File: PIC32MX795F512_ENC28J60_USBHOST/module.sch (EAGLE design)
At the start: 75 parts, among them IC1 IC_USBLC6-2, IC2 LM1117IMPX-3.3, IC3 PIC32MX795F512, IC4 ENC28J60, T1 BC847, U1 USD-SOCKETUSD, X1 22-23-2021, X2 CRYSTALS-NOGND-CFPX-217, X3 KUSBVX, X4 22-23-2021, X5 22-23-2021, Y1 CRYSTAL-GROUNDEDSMD-5X3.2, Y2 CRYSTAL-GROUNDEDSMD-5X3.2

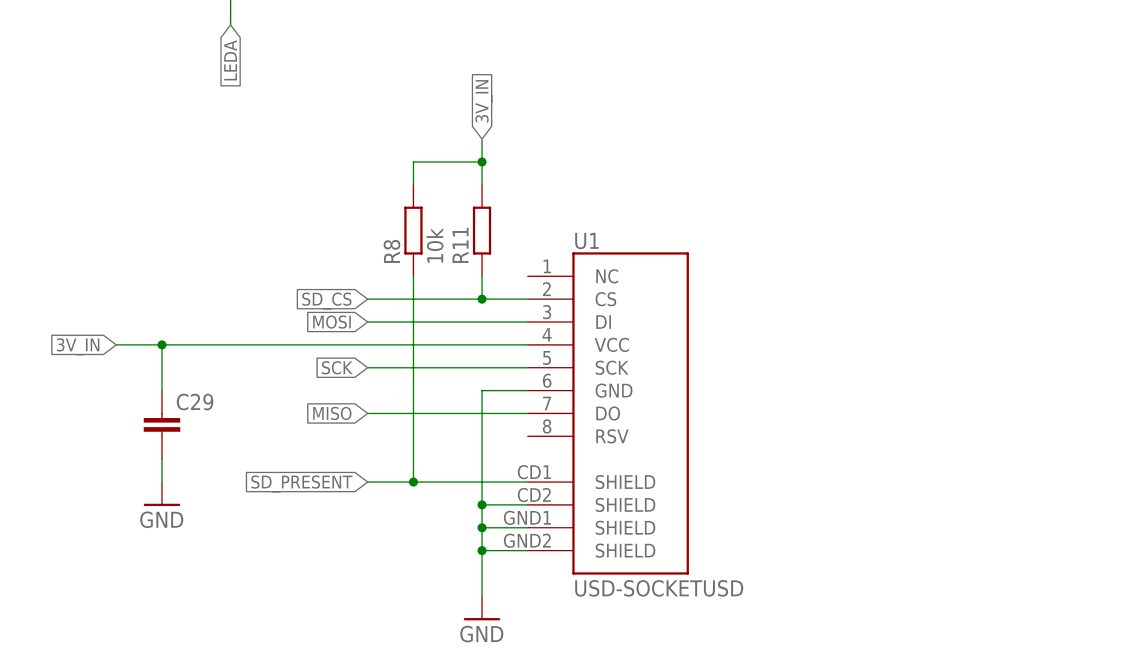
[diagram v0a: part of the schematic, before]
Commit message: MISO pull-ups added
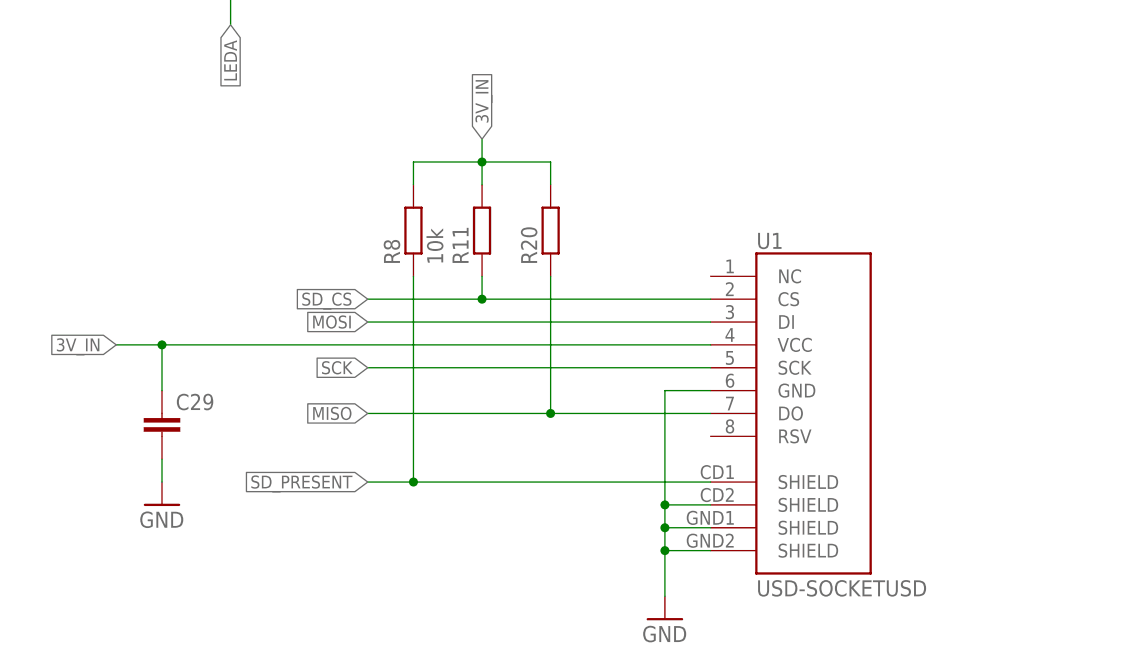
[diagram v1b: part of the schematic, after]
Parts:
- added R20: (no value), rcl:R-EU_R0603
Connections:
- net 3V_IN: now also R20.2
- net MISO: now also R20.1
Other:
- moved on the sheet: U1
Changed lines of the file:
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@@
 <part name="GND51" library="SparkFun-Aesthetics" deviceset="GND" device=""/>
 <part name="R18" library="rcl" deviceset="R-EU_" device="R0805"/>
+<part name="R20" library="rcl" deviceset="R-EU_" device="R0603"/>
 </parts>
 <sheets>
@@
 <instance part="R12" gate="G$1" x="73.66" y="83.82"/>
 <instance part="Y2" gate="G$1" x="73.66" y="157.48" rot="R90"/>
-<instance part="U1" gate="G$1" x="254" y="81.28"/>
-<instance part="GND47" gate="1" x="241.3" y="55.88"/>
+<instance part="U1" gate="G$1" x="274.32" y="81.28"/>
+<instance part="GND47" gate="1" x="261.62" y="55.88"/>
 <instance part="R11" gate="G$1" x="241.3" y="99.06" rot="R90"/>
 <instance part="C29" gate="G$1" x="205.74" y="78.74"/>
@@
 <instance part="GND51" gate="1" x="-53.34" y="535.94" rot="MR0"/>
 <instance part="R18" gate="G$1" x="104.14" y="520.7"/>
+<instance part="R20" gate="G$1" x="248.92" y="99.06" rot="R90"/>
 </instances>
 <busses>
@@
 <pinref part="GND47" gate="1" pin="GND"/>
 <pinref part="U1" gate="G$1" pin="SHIELD@4"/>
-<wire x1="241.3" y1="66.04" x2="241.3" y2="63.5" width="0.1524" layer="91"/>
-<wire x1="241.3" y1="63.5" x2="241.3" y2="58.42" width="0.1524" layer="91"/>
-<wire x1="246.38" y1="63.5" x2="241.3" y2="63.5" width="0.1524" layer="91"/>
-<junction x="241.3" y="63.5"/>
+<wire x1="261.62" y1="66.04" x2="261.62" y2="63.5" width="0.1524" layer="91"/>
+<wire x1="261.62" y1="63.5" x2="261.62" y2="58.42" width="0.1524" layer="91"/>
+<wire x1="266.7" y1="63.5" x2="261.62" y2="63.5" width="0.1524" layer="91"/>
+<junction x="261.62" y="63.5"/>
 <pinref part="U1" gate="G$1" pin="SHIELD@3"/>
-<wire x1="246.38" y1="66.04" x2="241.3" y2="66.04" width="0.1524" layer="91"/>
-<junction x="241.3" y="66.04"/>
+<wire x1="266.7" y1="66.04" x2="261.62" y2="66.04" width="0.1524" layer="91"/>
+<junction x="261.62" y="66.04"/>
 <pinref part="U1" gate="G$1" pin="GND"/>
-<wire x1="246.38" y1="81.28" x2="241.3" y2="81.28" width="0.1524" layer="91"/>
-<wire x1="241.3" y1="81.28" x2="241.3" y2="68.58" width="0.1524" layer="91"/>
+<wire x1="266.7" y1="81.28" x2="261.62" y2="81.28" width="0.1524" layer="91"/>
+<wire x1="261.62" y1="81.28" x2="261.62" y2="68.58" width="0.1524" layer="91"/>
 <pinref part="U1" gate="G$1" pin="SHIELD@2"/>
-<wire x1="241.3" y1="68.58" x2="241.3" y2="66.04" width="0.1524" layer="91"/>
-<wire x1="246.38" y1="68.58" x2="241.3" y2="68.58" width="0.1524" layer="91"/>
-<junction x="241.3" y="68.58"/>
+<wire x1="261.62" y1="68.58" x2="261.62" y2="66.04" width="0.1524" layer="91"/>
+<wire x1="266.7" y1="68.58" x2="261.62" y2="68.58" width="0.1524" layer="91"/>
+<junction x="261.62" y="68.58"/>
 </segment>
 <segment>
@@
 <segment>
 <pinref part="U1" gate="G$1" pin="SCK"/>
-<wire x1="246.38" y1="83.82" x2="228.6" y2="83.82" width="0.1524" layer="91"/>
+<wire x1="266.7" y1="83.82" x2="228.6" y2="83.82" width="0.1524" layer="91"/>
 <label x="228.6" y="83.82" size="1.4224" layer="95" rot="R180" xref="yes"/>
 </segment>
@@
 <segment>
 <pinref part="U1" gate="G$1" pin="DO"/>
-<wire x1="246.38" y1="78.74" x2="228.6" y2="78.74" width="0.1524" layer="91"/>
+<wire x1="266.7" y1="78.74" x2="248.92" y2="78.74" width="0.1524" layer="91"/>
 <label x="228.6" y="78.74" size="1.4224" layer="95" rot="R180" xref="yes"/>
+<pinref part="R20" gate="G$1" pin="1"/>
+<wire x1="248.92" y1="78.74" x2="228.6" y2="78.74" width="0.1524" layer="91"/>
+<wire x1="248.92" y1="93.98" x2="248.92" y2="78.74" width="0.1524" layer="91"/>
+<junction x="248.92" y="78.74"/>
 </segment>
 <segment>
@@
 <segment>
 <pinref part="U1" gate="G$1" pin="DI"/>
-<wire x1="246.38" y1="88.9" x2="228.6" y2="88.9" width="0.1524" layer="91"/>
+<wire x1="266.7" y1="88.9" x2="228.6" y2="88.9" width="0.1524" layer="91"/>
 <label x="228.6" y="88.9" size="1.4224" layer="95" rot="R180" xref="yes"/>
 </segment>
@@
 <segment>
 <pinref part="U1" gate="G$1" pin="CS"/>
-<wire x1="246.38" y1="91.44" x2="241.3" y2="91.44" width="0.1524" layer="91"/>
+<wire x1="266.7" y1="91.44" x2="241.3" y2="91.44" width="0.1524" layer="91"/>
 <pinref part="R11" gate="G$1" pin="1"/>
 <wire x1="241.3" y1="91.44" x2="228.6" y2="91.44" width="0.1524" layer="91"/>
@@
 <segment>
 <pinref part="U1" gate="G$1" pin="SHIELD@1"/>
-<wire x1="246.38" y1="71.12" x2="233.68" y2="71.12" width="0.1524" layer="91"/>
+<wire x1="266.7" y1="71.12" x2="233.68" y2="71.12" width="0.1524" layer="91"/>
 <label x="228.6" y="71.12" size="1.4224" layer="95" rot="R180" xref="yes"/>
 <pinref part="R8" gate="G$1" pin="1"/>
@@
 <segment>
 <pinref part="U1" gate="G$1" pin="VCC"/>
-<wire x1="246.38" y1="86.36" x2="205.74" y2="86.36" width="0.1524" layer="91"/>
+<wire x1="266.7" y1="86.36" x2="205.74" y2="86.36" width="0.1524" layer="91"/>
 <pinref part="C29" gate="G$1" pin="1"/>
 <wire x1="205.74" y1="86.36" x2="200.66" y2="86.36" width="0.1524" layer="91"/>
@@
 <pinref part="R8" gate="G$1" pin="2"/>
 <wire x1="233.68" y1="106.68" x2="233.68" y2="104.14" width="0.1524" layer="91"/>
-</segment>
-<segment>
+<pinref part="R20" gate="G$1" pin="2"/>
+<wire x1="241.3" y1="106.68" x2="248.92" y2="106.68" width="0.1524" layer="91"/>
+<wire x1="248.92" y1="106.68" x2="248.92" y2="104.14" width="0.1524" layer="91"/>
+</segment>
+<segment>
